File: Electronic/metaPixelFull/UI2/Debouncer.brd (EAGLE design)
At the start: 67.9 x 58.1 mm, 31 parts, among them IC1 74HCT14N, IC2 74HCT14N, Q1 2N3906

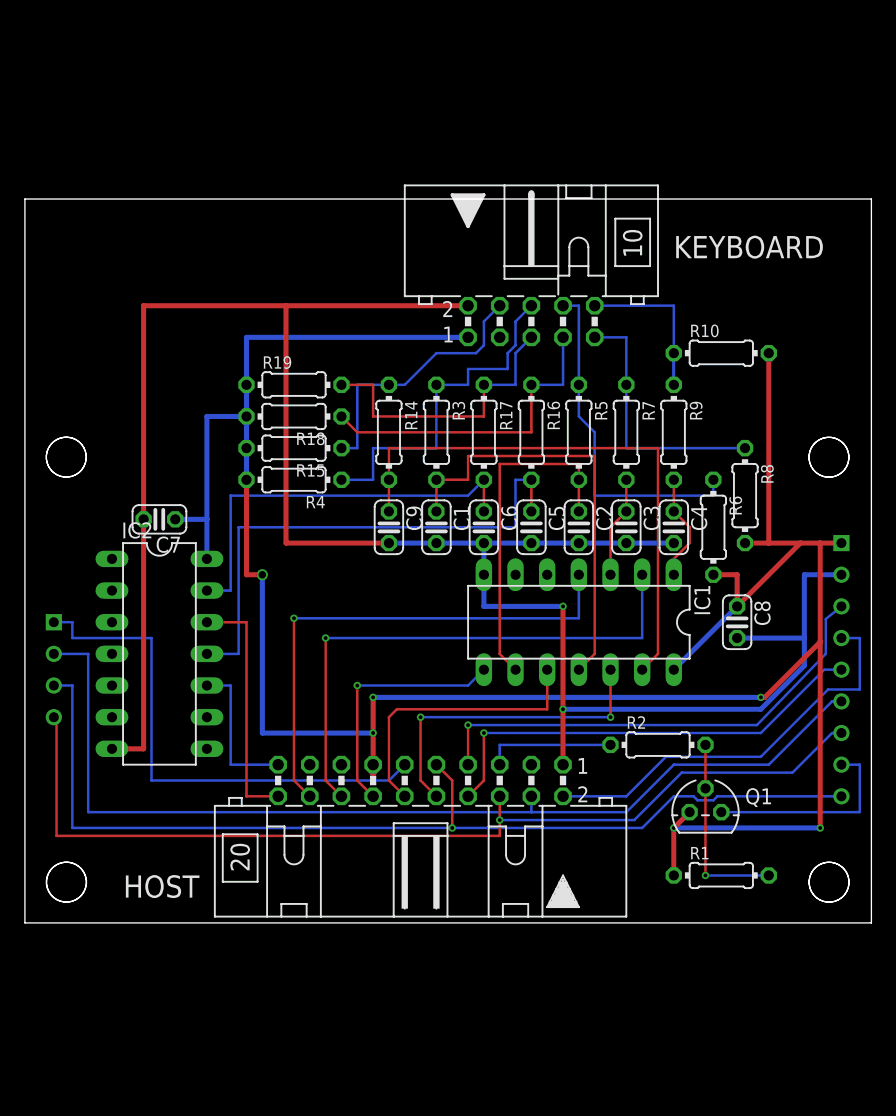
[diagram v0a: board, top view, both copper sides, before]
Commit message: Removing the TFT from the Debouncer
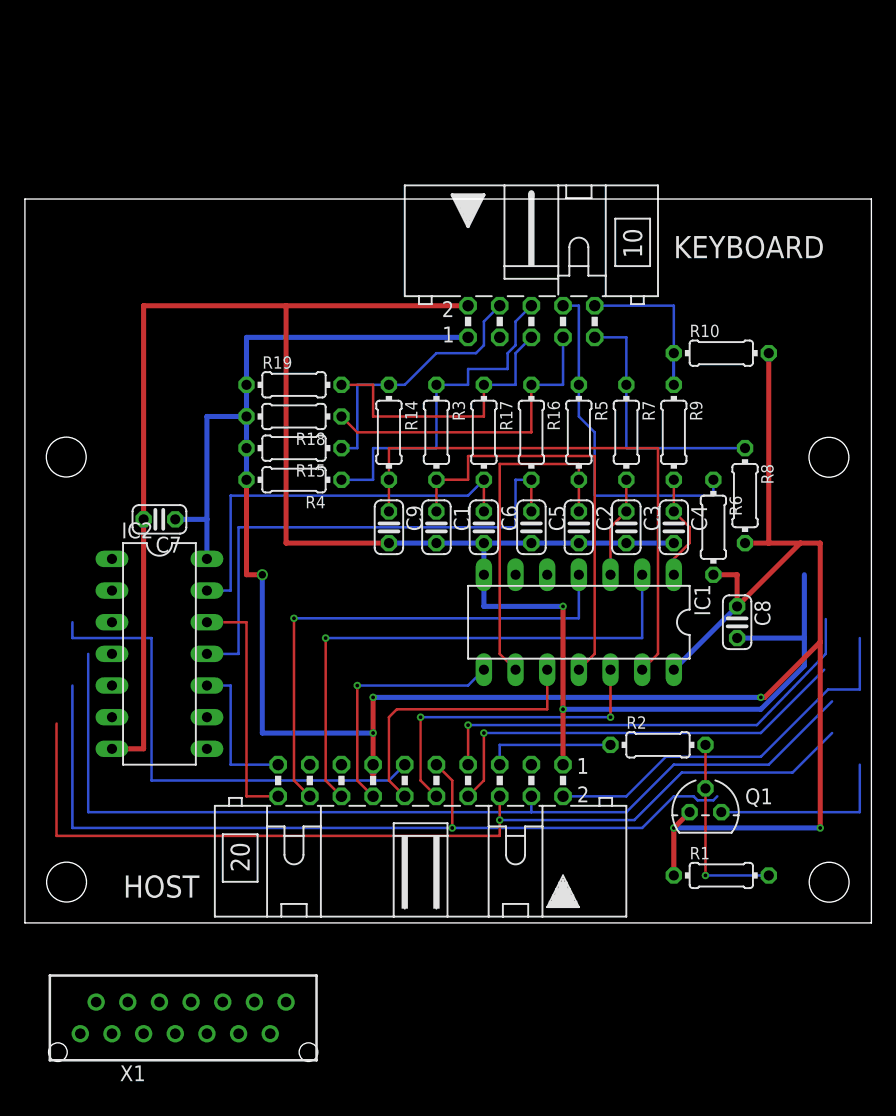
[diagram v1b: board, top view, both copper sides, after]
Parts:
- removed U$1: 2.2_TFT_LCDNEW, 2.2"tft:2.2_TFT_LCD_LEDSEE
- added X1: MICS-14, con-lumberg:MICS-14
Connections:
- net !LCD_CS: no longer U$1.P$3_CS
- net !LCD_RST: no longer U$1.P$2_RESET
- net !MEM_CS: no longer U$1.P$2_SD_CS
- net +3.3V: no longer U$1.P$5_VCC
- net BG_LED: no longer U$1.P$8_LED
- net GND: no longer U$1.P$4_GND
- net LCD_DC: no longer U$1.P$1_DC
- net MISO: no longer U$1.P$3_SD_MISO, U$1.P$9_MISO
- net MOSI: no longer U$1.P$1_SD_MOSI, U$1.P$6_MOSI
- net SCLK: no longer U$1.P$4_SD_SCK, U$1.P$7_SCK
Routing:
- net MISO: track 81.6 -> 70.1 mm
- net MOSI: track 80.9 -> 77.3 mm
- net GND: track 174.9 -> 171.9 mm
- net +3.3V: track 202.6 -> 200.9 mm
- net !LCD_CS: track 38.7 -> 37.1 mm
- net !MEM_CS: track 41.4 -> 39.9 mm
- net BG_LED: track 16.4 -> 14.9 mm
- net !LCD_RST: track 33.0 -> 31.5 mm
- net LCD_DC: track 36.4 -> 35.0 mm
- net SCLK: track 78.6 -> 77.3 mm
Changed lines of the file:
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@@
 <attribute name="VALUE" x="36.8554" y="0" size="1.778" layer="27" ratio="10" rot="R180"/>
 </element>
-<element name="U$1" library="2.2&quot;tft" package="2.2_TFT_LCD_LEDSEE" value="2.2_TFT_LCDNEW" x="33.92" y="20.32" rot="MR0"/>
 <element name="C9" library="rcl" package="C025-024X044" value=".1µ" x="29.21" y="31.75" rot="R270"/>
 <element name="R14" library="resistor" package="0204/7" value="15k" x="29.21" y="39.37" rot="R270"/>
@@
 <element name="C7" library="rcl" package="C025-024X044" value=".1µ" x="10.795" y="32.385" rot="R180"/>
 <element name="C8" library="rcl" package="C025-024X044" value=".1µ" x="57.15" y="24.13" rot="R270"/>
+<element name="X1" library="con-lumberg" package="MICS-14" value="MICS-14" x="12.7" y="-7.62">
+<attribute name="MPN" value="" x="12.7" y="-7.62" size="1.778" layer="27" display="off"/>
+<attribute name="OC_FARNELL" value="unknown" x="12.7" y="-7.62" size="1.778" layer="27" display="off"/>
+<attribute name="OC_NEWARK" value="unknown" x="12.7" y="-7.62" size="1.778" layer="27" display="off"/>
+<attribute name="MF" value="" x="12.7" y="-7.62" size="1.778" layer="27" display="off"/>
+</element>
 </elements>
 <signals>
@@
 <signal name="GND" class="1">
 <contactref element="HOST" pad="1"/>
-<contactref element="U$1" pad="P$4_GND"/>
 <contactref element="IC1" pad="7"/>
 <contactref element="IC2" pad="7"/>
@@
 <wire x1="62.5475" y1="20.6375" x2="62.5475" y2="22.86" width="0.4064" layer="16"/>
 <wire x1="62.5475" y1="22.86" x2="62.5475" y2="27.94" width="0.4064" layer="16"/>
-<wire x1="62.5475" y1="27.94" x2="65.52" y2="27.94" width="0.4064" layer="16"/>
 <wire x1="36.83" y1="25.4" x2="36.83" y2="27.94" width="0.4064" layer="16"/>
 <wire x1="43.18" y1="17.145" x2="43.18" y2="25.4" width="0.4064" layer="1"/>
@@
 <signal name="!LCD_CS">
 <contactref element="HOST" pad="7"/>
-<contactref element="U$1" pad="P$3_CS"/>
 <wire x1="35.56" y1="12.7" x2="35.56" y2="15.875" width="0.2032" layer="1"/>
 <via x="35.56" y="15.875" extent="1-16" drill="0.3048" diameter="0.254"/>
@@
 <wire x1="58.7375" y1="15.875" x2="64.262" y2="21.59" width="0.2032" layer="16"/>
 <wire x1="64.262" y1="21.59" x2="64.262" y2="24.384" width="0.2032" layer="16"/>
-<wire x1="64.262" y1="24.384" x2="65.52" y2="25.4" width="0.2032" layer="16"/>
 </signal>
 <signal name="MISO">
 <contactref element="HOST" pad="9"/>
-<contactref element="U$1" pad="P$9_MISO"/>
-<contactref element="U$1" pad="P$3_SD_MISO"/>
-<wire x1="2.32" y1="19.05" x2="3.81" y2="19.05" width="0.2032" layer="16"/>
 <wire x1="3.81" y1="19.05" x2="3.81" y2="7.62" width="0.2032" layer="16"/>
 <wire x1="34.29" y1="11.43" x2="33.02" y2="12.7" width="0.2032" layer="1"/>
@@
 <via x="34.29" y="7.62" extent="1-16" drill="0.3048" diameter="0.254"/>
 <wire x1="34.29" y1="7.62" x2="34.29" y2="11.43" width="0.2032" layer="1"/>
-<wire x1="65.52" y1="10.16" x2="55.5625" y2="10.16" width="0.2032" layer="16"/>
 <wire x1="55.5625" y1="10.16" x2="55.245" y2="9.8425" width="0.2032" layer="16"/>
 <wire x1="55.245" y1="9.8425" x2="53.975" y2="9.8425" width="0.2032" layer="16"/>
@@
 <contactref element="Q1" pad="3"/>
 <contactref element="R1" pad="1"/>
-<contactref element="U$1" pad="P$5_VCC"/>
 <contactref element="KEYBOARD" pad="1"/>
 <contactref element="R18" pad="2"/>
@@
 <wire x1="52.07" y1="3.81" x2="52.07" y2="7.62" width="0.4064" layer="1"/>
 <wire x1="52.07" y1="7.62" x2="53.34" y2="8.89" width="0.4064" layer="1"/>
-<wire x1="65.52" y1="30.48" x2="63.8175" y2="30.48" width="0.4064" layer="1"/>
 <wire x1="63.8175" y1="7.62" x2="52.07" y2="7.62" width="0.4064" layer="16"/>
 <via x="63.8175" y="7.62" extent="1-16" drill="0.3048" diameter="0.254"/>
@@
 <signal name="!LCD_RST">
 <contactref element="HOST" pad="2"/>
-<contactref element="U$1" pad="P$2_RESET"/>
 <wire x1="43.18" y1="10.16" x2="48.26" y2="10.16" width="0.2032" layer="16"/>
 <wire x1="48.26" y1="10.16" x2="51.435" y2="13.335" width="0.2032" layer="16"/>
@@
 <wire x1="64.4525" y1="18.7325" x2="66.9925" y2="18.7325" width="0.2032" layer="16"/>
 <wire x1="66.9925" y1="18.7325" x2="66.9925" y2="22.86" width="0.2032" layer="16"/>
-<wire x1="66.9925" y1="22.86" x2="65.52" y2="22.86" width="0.2032" layer="16"/>
 </signal>
 <signal name="MOSI">
 <contactref element="HOST" pad="4"/>
-<contactref element="U$1" pad="P$6_MOSI"/>
-<contactref element="U$1" pad="P$1_SD_MOSI"/>
-<wire x1="2.32" y1="21.59" x2="5.08" y2="21.59" width="0.2032" layer="16"/>
 <wire x1="5.08" y1="21.59" x2="5.08" y2="8.89" width="0.2032" layer="16"/>
 <wire x1="5.08" y1="8.89" x2="40.64" y2="8.89" width="0.2032" layer="16"/>
 <wire x1="40.64" y1="8.89" x2="48.26" y2="8.89" width="0.2032" layer="16"/>
-<wire x1="65.52" y1="17.78" x2="64.77" y2="17.78" width="0.2032" layer="16"/>
 <wire x1="64.77" y1="17.78" x2="59.69" y2="12.7" width="0.2032" layer="16"/>
 <wire x1="59.69" y1="12.7" x2="52.07" y2="12.7" width="0.2032" layer="16"/>
@@
 <signal name="SCLK">
 <contactref element="HOST" pad="6"/>
-<contactref element="U$1" pad="P$7_SCK"/>
-<contactref element="U$1" pad="P$4_SD_SCK"/>
 <wire x1="2.54" y1="6.985" x2="38.1" y2="6.985" width="0.2032" layer="1"/>
 <wire x1="38.1" y1="6.985" x2="38.1" y2="8.255" width="0.2032" layer="1"/>
 <wire x1="38.1" y1="8.255" x2="38.1" y2="10.16" width="0.2032" layer="1"/>
-<wire x1="65.52" y1="15.24" x2="64.77" y2="15.24" width="0.2032" layer="16"/>
 <wire x1="64.77" y1="15.24" x2="61.595" y2="12.065" width="0.2032" layer="16"/>
 <wire x1="61.595" y1="12.065" x2="52.705" y2="12.065" width="0.2032" layer="16"/>
@@
 <wire x1="48.895" y1="8.255" x2="38.1" y2="8.255" width="0.2032" layer="16"/>
 <via x="38.1" y="8.255" extent="1-16" drill="0.3048" diameter="0.254"/>
-<wire x1="2.32" y1="16.51" x2="2.54" y2="16.002" width="0.2032" layer="1"/>
 <wire x1="2.54" y1="16.002" x2="2.54" y2="6.985" width="0.2032" layer="1"/>
 </signal>
 <signal name="LCD_DC">
 <contactref element="HOST" pad="8"/>
-<contactref element="U$1" pad="P$1_DC"/>
 <wire x1="35.56" y1="10.16" x2="36.83" y2="11.43" width="0.2032" layer="1"/>
 <wire x1="36.83" y1="11.43" x2="36.83" y2="15.24" width="0.2032" layer="1"/>
-<wire x1="65.52" y1="20.32" x2="64.135" y2="20.32" width="0.2032" layer="16"/>
 <wire x1="64.135" y1="20.32" x2="59.055" y2="15.24" width="0.2032" layer="16"/>
 <wire x1="59.055" y1="15.24" x2="36.83" y2="15.24" width="0.2032" layer="16"/>
@@
 <signal name="!MEM_CS">
 <contactref element="HOST" pad="11"/>
-<contactref element="U$1" pad="P$2_SD_CS"/>
-<wire x1="2.32" y1="24.13" x2="3.81" y2="24.13" width="0.2032" layer="16"/>
 <wire x1="3.81" y1="24.13" x2="3.81" y2="22.86" width="0.2032" layer="16"/>
 <wire x1="3.81" y1="22.86" x2="10.16" y2="22.86" width="0.2032" layer="16"/>
@@
 </signal>
 <signal name="BG_LED">
-<contactref element="U$1" pad="P$8_LED"/>
 <contactref element="Q1" pad="1"/>
-<wire x1="65.52" y1="12.7" x2="66.9925" y2="12.7" width="0.2032" layer="16"/>
 <wire x1="66.9925" y1="12.7" x2="66.9925" y2="8.89" width="0.2032" layer="16"/>
 <wire x1="66.9925" y1="8.89" x2="55.88" y2="8.89" width="0.2032" layer="16"/>

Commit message: Restructure Hardware
prepare for an TFT only adapter board
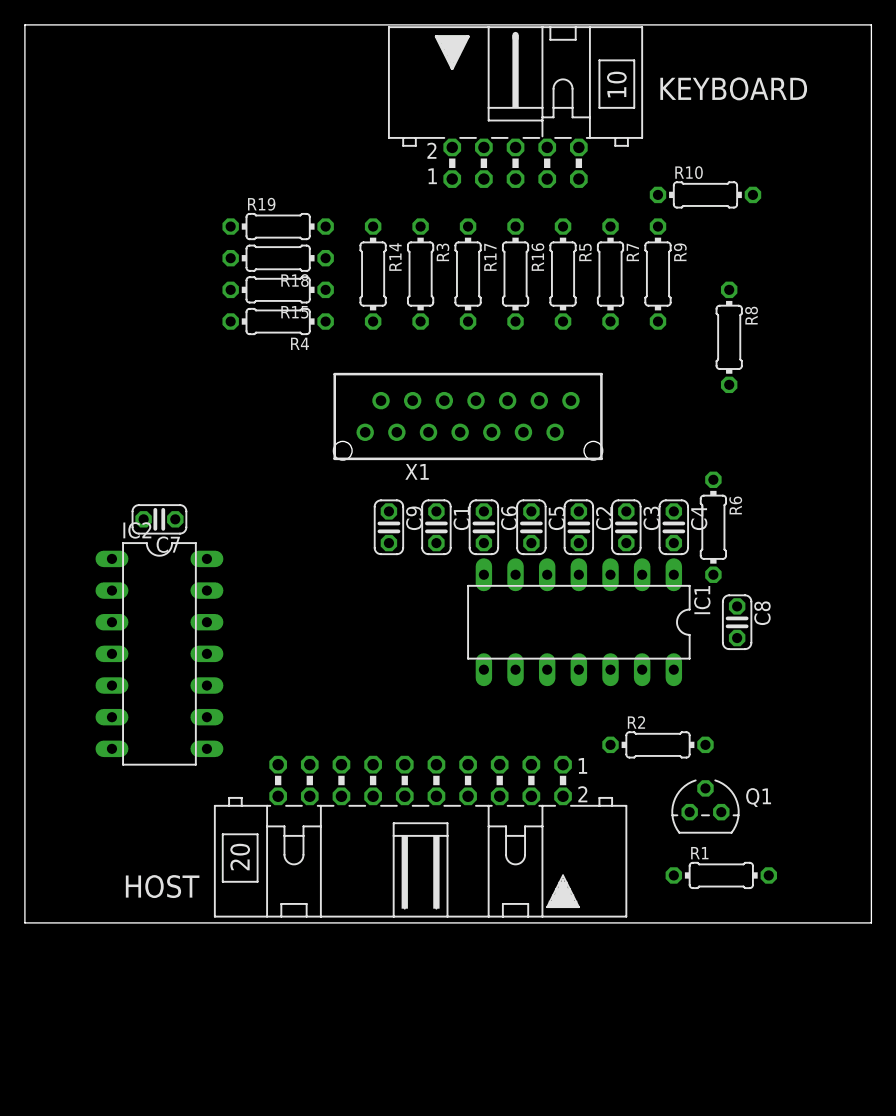
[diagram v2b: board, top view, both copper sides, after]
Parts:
- moved X1 53.4 mm to (35.6, 40.6)
- moved KEYBOARD 12.8 mm to (39.4, 61.0)
- moved R10 12.8 mm to (54.6, 58.4)
- moved R14 12.8 mm to (27.9, 52.1)
- moved R16 12.8 mm to (39.4, 52.1)
- moved R17 12.8 mm to (35.6, 52.1)
- moved R18 12.8 mm to (20.3, 53.3)
- moved R19 12.8 mm to (20.3, 55.9)
- moved R3 12.8 mm to (31.8, 52.1)
- moved R5 12.8 mm to (43.2, 52.1)
- moved R7 12.8 mm to (47.0, 52.1)
- moved R8 12.8 mm to (56.5, 47.0)
- moved R9 12.8 mm to (50.8, 52.1)
- moved R15 12.8 mm to (20.3, 50.8)
- moved R4 12.8 mm to (20.3, 48.3)
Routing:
- net +3.3V: track 200.9 -> 0.00 mm, vias 6 -> 0
- net GND: track 171.9 -> 0.00 mm, vias 2 -> 0
- net MOSI: track 77.3 -> 0.00 mm
- net SCLK: track 77.3 -> 0.00 mm, vias 1 -> 0
- net MISO: track 70.1 -> 0.00 mm, vias 1 -> 0
- net K1: track 45.0 -> 0.00 mm
- net KEY_4: track 43.7 -> 0.00 mm, vias 1 -> 0
- net ENC1: track 42.5 -> 0.00 mm
- net KEY_5: track 41.2 -> 0.00 mm, vias 1 -> 0
- net !MEM_CS: track 39.9 -> 0.00 mm
- net !LCD_CS: track 37.1 -> 0.00 mm, vias 1 -> 0
- net LCD_DC: track 35.0 -> 0.00 mm, vias 1 -> 0
- net K2: track 34.8 -> 0.00 mm
- net ENC2: track 32.9 -> 0.00 mm
- net !LCD_RST: track 31.5 -> 0.00 mm
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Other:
- board size 67.9 x 58.1 mm -> 67.9 x 72.1 mm
